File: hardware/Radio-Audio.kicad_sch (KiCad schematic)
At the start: 13 parts, among them U1 LM386, U2 RDA5807M_Module

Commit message: Reduced Component Sizes + Added Mounting Holes
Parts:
- C2, C3, C4: footprint Capacitor_SMD:C_1812_4532Metric -> Capacitor_SMD:C_1206_3216Metric
- R1, R2, R3, R4: footprint Resistor_SMD:R_1812_4532Metric -> Resistor_SMD:R_1206_3216Metric
- U2: footprint ECE:RDA5807M_Module_TH -> ECE:RDA5807M_Module_SM
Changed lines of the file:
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@@
 			)
 		)
-		(property "Footprint" "Capacitor_SMD:C_1812_4532Metric"
+		(property "Footprint" "Capacitor_SMD:C_1206_3216Metric"
 			(at 170.18 81.28 0)
 			(effects
@@
 			)
 		)
-		(property "Footprint" "Resistor_SMD:R_1812_4532Metric"
+		(property "Footprint" "Resistor_SMD:R_1206_3216Metric"
 			(at 187.706 117.094 90)
 			(effects
@@
 			)
 		)
-		(property "Footprint" "Capacitor_SMD:C_1812_4532Metric"
+		(property "Footprint" "Capacitor_SMD:C_1206_3216Metric"
 			(at 186.69 107.95 0)
 			(effects
@@
 			)
 		)
-		(property "Footprint" "Resistor_SMD:R_1812_4532Metric"
+		(property "Footprint" "Resistor_SMD:R_1206_3216Metric"
 			(at 145.796 100.584 90)
 			(effects
@@
 			)
 		)
-		(property "Footprint" "Resistor_SMD:R_1812_4532Metric"
+		(property "Footprint" "Resistor_SMD:R_1206_3216Metric"
 			(at 75.184 78.486 90)
 			(effects
@@
 			)
 		)
-		(property "Footprint" "Resistor_SMD:R_1812_4532Metric"
+		(property "Footprint" "Resistor_SMD:R_1206_3216Metric"
 			(at 67.056 78.994 90)
 			(effects
@@
 			)
 		)
-		(property "Footprint" "ECE:RDA5807M_Module_TH"
+		(property "Footprint" "ECE:RDA5807M_Module_SM"
 			(at 92.71 96.52 0)
 			(effects
@@
 			)
 		)
-		(property "Footprint" "Capacitor_SMD:C_1812_4532Metric"
+		(property "Footprint" "Capacitor_SMD:C_1206_3216Metric"
 			(at 138.43 93.98 0)
 			(effects

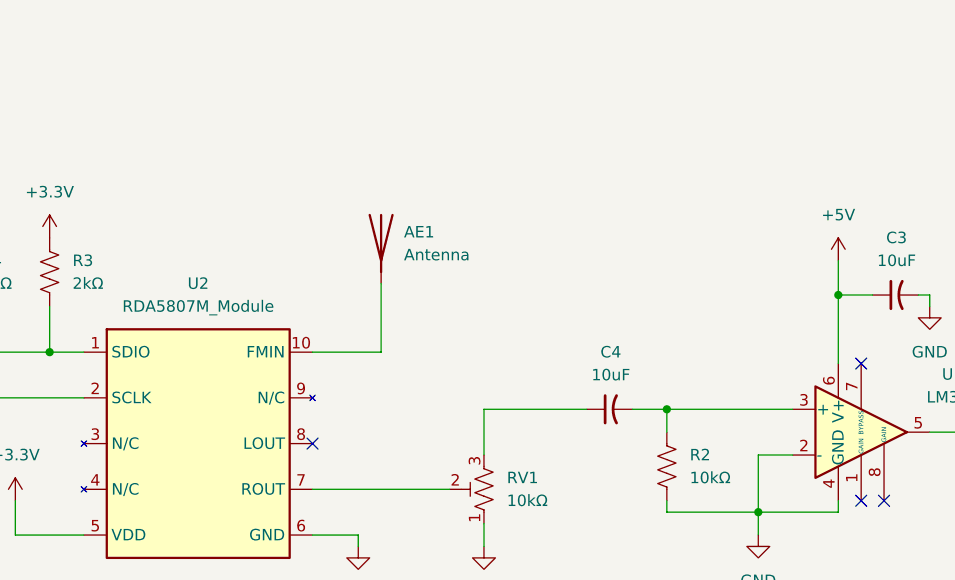
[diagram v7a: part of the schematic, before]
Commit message: PWM Audio, Power fix
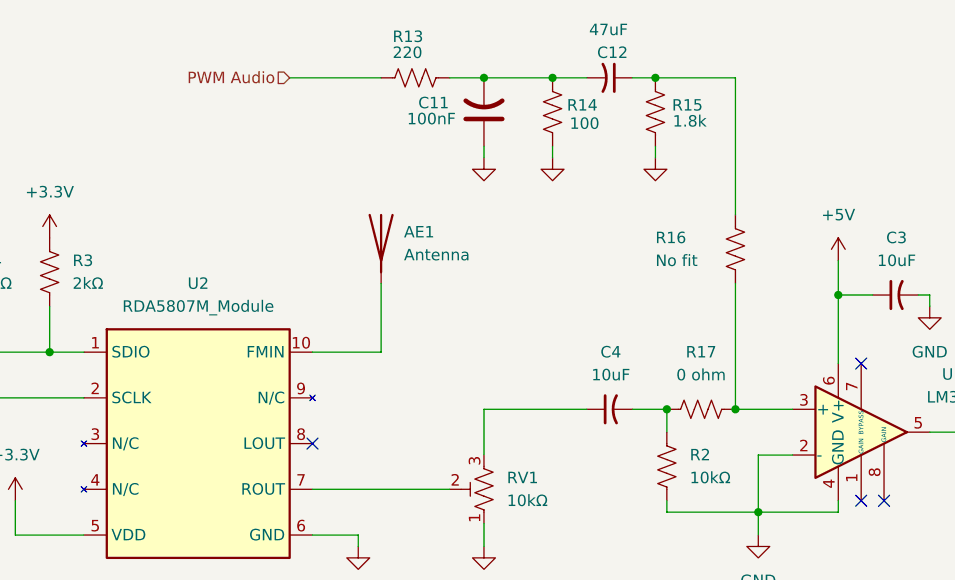
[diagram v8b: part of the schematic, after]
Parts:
- added C11: 100nF, symbol Device:C_US
- added C12: 47uF, symbol Device:C_Small_US
- added R13: 220, symbol Device:R_US
- added R14: 100, symbol Device:R_US
- added R15: 1.8k, symbol Device:R_US
- added R16: No fit, symbol Device:R_US
- added R17: 0 ohm, symbol Device:R_US
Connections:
- net GND: now also C11.1, R14.1, R15.1
- net at C4.2, R2.1: now also R17.1; no longer U1.3 (+)
- new net: C11.2, C12.2, R13.1, R14.2
- new net: C12.1, R15.2, R16.1
- new net: R16.2, R17.2, U1.3 (+)
- new net PWM Audio: R13.2
